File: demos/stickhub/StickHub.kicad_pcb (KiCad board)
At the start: 2 copper layers, 16.5 x 40 mm, 94 parts, among them J1 HOST, J2 USB1, J3 USB2, J4 USB3, J5 USB4, J6 USB5, J7 USB6, J8 USB7, J9 EXTGND, U1 MaxLinear_XR22417-48, U2 Dialog_SLG5NT1487V, Y1 12MHz 50ppm 16-20pF

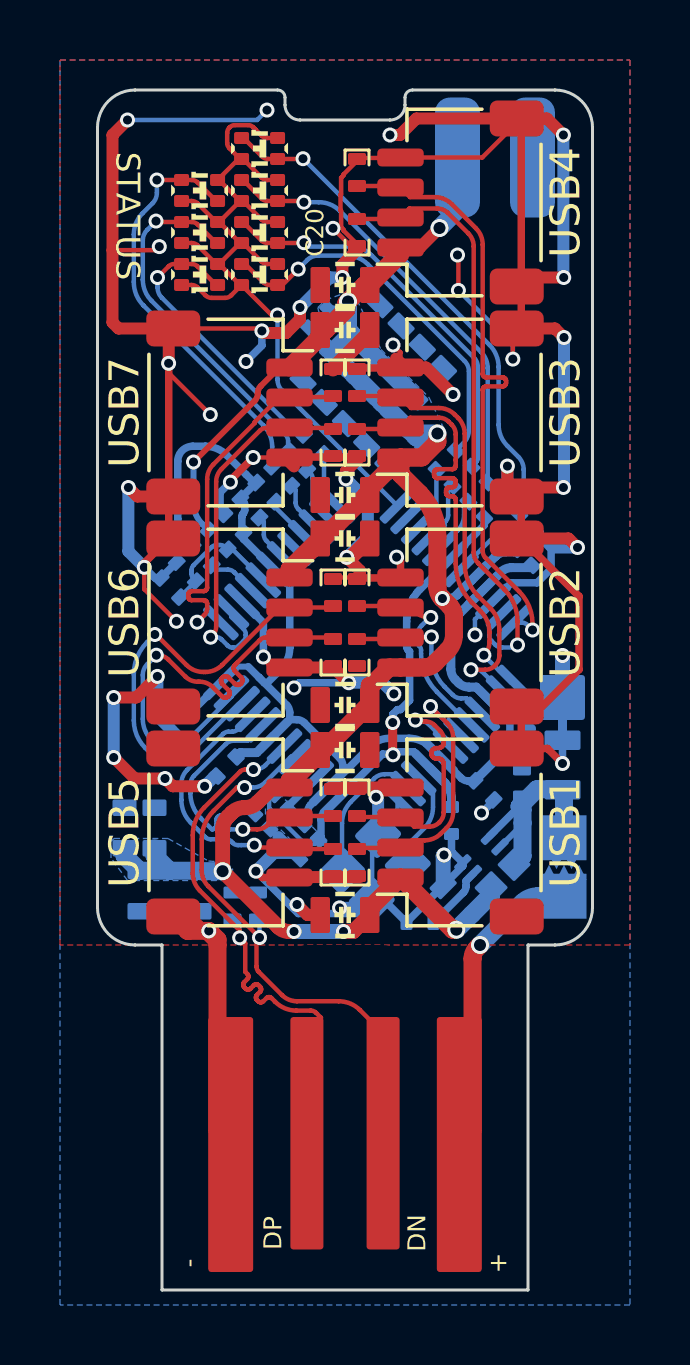
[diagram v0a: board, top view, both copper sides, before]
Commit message: feat: update kicad to 9.0.0+dfsg-1
Signed-off-by: lhdjply <lhdjply@126.com>
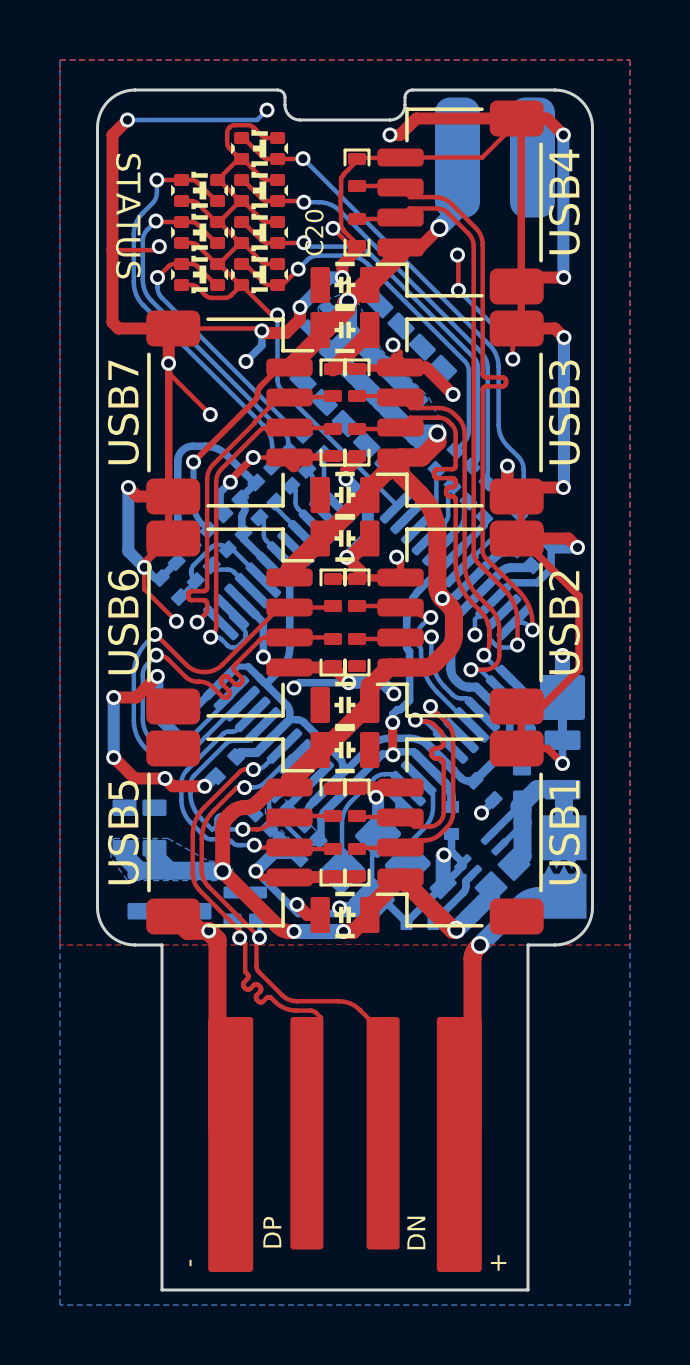
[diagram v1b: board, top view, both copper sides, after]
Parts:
- C1, C10, C11, C12, C13, C2, C28, C3, C4, C5, C6, C7, C8, C9: footprint Capacitor_SMD:1005_C -> footprints:1005_C
- C14, C15, C16, C17, C18, C19, C20, C21: footprint Capacitor_SMD:2012_C -> footprints:2012_C
- C22, C23, C24, C25, C26, C27, C29, C30, C31, C32, C33, C34, C35, C36, C37: footprint Capacitor_SMD:1608_C -> footprints:1608_C
- C38: footprint Capacitor_SMD:CP_Elec_6.3x11_Board_Edge_Mirrored -> footprints:CP_Elec_6.3x11_Board_Edge_Mirrored
- D15, D16, D17, D18, D19, D20, D21: footprint LED_SMD:Duo_LED_1.6x0.8_Kingbright_APHB1608LZGKSURKC -> footprints:Duo_LED_1.6x0.8_Kingbright_APHB1608LZGKSURKC
- H1: footprint MountingHole:Plain_Hole_3mm -> footprints:Plain_Hole_3mm
- J1: footprint Connector_USB:USB_A_PCB_traces_small -> footprints:USB_A_PCB_traces_small
- J2, J3, J4, J5, J6, J7, J8: footprint Connector_JST:JST_SH_SM04B-SRSS-TB_1x04-1MP_P1.00mm_Horizontal -> footprints:JST_SH_SM04B-SRSS-TB_1x04-1MP_P1.00mm_Horizontal
- J9: footprint SH_Solder_Pads:1P-1.5x1.5 -> footprints:1P-1.5x1.5
- JP1: footprint SH_Solder_Pads:JP-2_1.5x1.5 -> footprints:JP-2_1.5x1.5
- LOGO1: footprint Symbol:Creative_Commons_CC_Mask -> footprints:Creative_Commons_CC_Mask
- LOGO2: footprint Symbol:Creative_Commons_BY_Mask -> footprints:Creative_Commons_BY_Mask
- LOGO3: footprint Symbol:Creative_Commons_NC_Mask -> footprints:Creative_Commons_NC_Mask
- LOGO4: footprint Symbol:Creative_Commons_SA_Mask -> footprints:Creative_Commons_SA_Mask
- U1: footprint Package_QFP:LQFP-48_7x7mm_P0.5mm -> footprints:LQFP-48_7x7mm_P0.5mm
- U2: footprint Package_DFN_QFN:TDFN-8_1.5x2mm_Fused-Lead_JEDEC_MO-252_W2015D -> footprints:TDFN-8_1.5x2mm_Fused-Lead_JEDEC_MO-252_W2015D
- Y1: footprint Crystal:Crystal_4-SMD_2.5x2mm -> footprints:Crystal_4-SMD_2.5x2mm
